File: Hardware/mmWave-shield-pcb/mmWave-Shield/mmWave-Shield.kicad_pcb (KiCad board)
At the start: 4 copper layers, 21 x 15 mm, 42 parts, among them J3 DF40HC_3.0_-40DS-0.4V_51, J4 DF40HC_3.0_-50DS-0.4V_51, U1 TPS22916CYFPR, U2 TPS22916CYFPR, X1 KC2016K80.0000C1GE00

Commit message: Cleaning up a bit
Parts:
- moved TP4 1.10 mm to (138.6, 105.2)
- moved TP5 1.10 mm to (139.7, 105.2)
- renumbered TP1 to DIV
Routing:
- net /sensor/sw_in_1v8: track 10.2 -> 11.4 mm
- net VD2: track 10.8 -> 11.8 mm
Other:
- board text added: "1V8"
- board text added: "3V3"

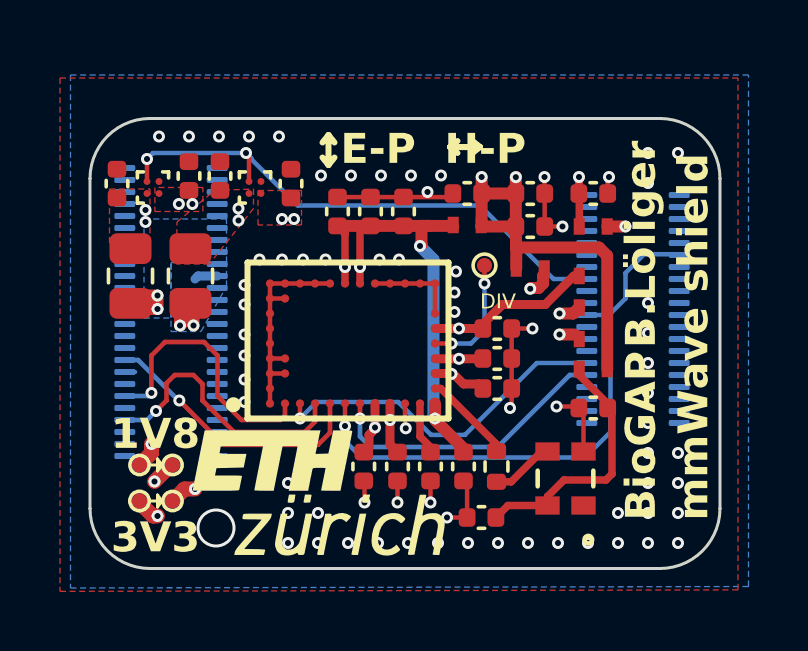
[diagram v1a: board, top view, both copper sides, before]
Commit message: Removed cap and rerouted some power lines
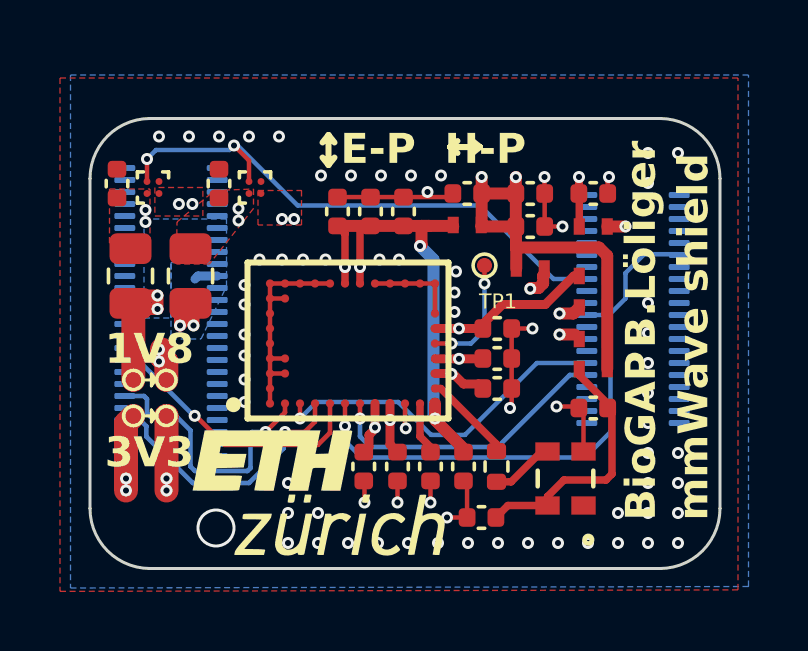
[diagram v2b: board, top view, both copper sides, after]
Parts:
- removed C17, C19: 47uF, Capacitor_SMD:C_0402_1005Metric
- C18, C20: value 1uF -> 4.7uF
- moved TP2 2.84 mm to (138.3, 103.6)
- moved TP3 2.84 mm to (139.4, 103.6)
- moved TP4 2.84 mm to (138.3, 102.4)
- moved TP5 2.84 mm to (139.4, 102.4)
- moved C20 0.26 mm to (141.2, 95.8)
- renumbered DIV to TP1
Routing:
- net /sensor/sw_in_1v8: track 11.4 -> 6.64 mm, vias 3 -> 4
- net 1V8_Connector: track 8.95 -> 4.84 mm, vias 3 -> 2
- net /sensor/sw_in_3v3: track 11.0 -> 12.9 mm, vias 3 -> 4
- net VD2: track 11.8 -> 12.8 mm, vias 3 -> 4
- net nRF_P0.07/AMUX: track 18.2 -> 18.8 mm

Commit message: added 3d models for new components
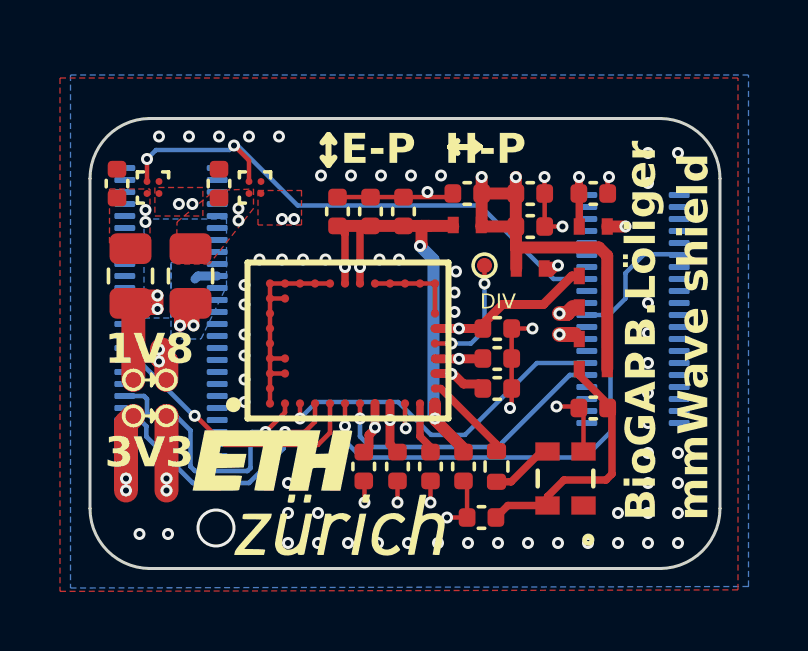
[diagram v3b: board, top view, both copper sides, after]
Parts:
- renumbered TP1 to DIV
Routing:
- net VDD_PLL: track 5.99 -> 7.13 mm
- net GND: vias 69 -> 71
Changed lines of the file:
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@@
 		)
 		(embedded_fonts no)
+		(model "${KIPRJMOD}/extra components/TPS22916CYFPR/TPS22916CYFPR.step"
+			(offset
+				(xyz 0 0 -0.2)
+			)
+			(scale
+				(xyz 1 1 1)
+			)
+			(rotate
+				(xyz -90 -0 -0)
+			)
+		)
 	)
 	(footprint "MMZ1005S121CT000:IND_1005_TDK-L"
@@
 		(descr "SMD pad as test Point, diameter 1.0mm")
 		(tags "test point SMD pad")
-		(property "Reference" "TP1"
+		(property "Reference" "DIV"
 			(at 0.45 1.2 0)
 			(layer "F.SilkS")
@@
 		)
 		(embedded_fonts no)
+		(model "${KIPRJMOD}/extra components/TPS22916CYFPR/TPS22916CYFPR.step"
+			(offset
+				(xyz 0 0 -0.2)
+			)
+			(scale
+				(xyz 1 1 1)
+			)
+			(rotate
+				(xyz -90 -0 -0)
+			)
+		)
 	)
 	(footprint "Resistor_SMD:R_0805_2012Metric"
@@
 		)
 		(embedded_fonts no)
+		(model "${KIPRJMOD}/extra components/KC2016K80_0000C1GE00/KC2016K_KYO.step"
+			(offset
+				(xyz 0 0 0)
+			)
+			(scale
+				(xyz 1 1 1)
+			)
+			(rotate
+				(xyz 0 0 0)
+			)
+		)
 	)
 	(footprint "Capacitor_SMD:C_0402_1005Metric"
@@
 	)
 	(via
+		(at 139.5 107.5)
+		(size 0.4)
+		(drill 0.2)
+		(layers "F.Cu" "B.Cu")
+		(free yes)
+		(net 2)
+	)
+	(via
 		(at 155.5 107.8)
 		(size 0.4)
@@
 	)
 	(via
+		(at 138.55 107.5)
+		(size 0.4)
+		(drill 0.2)
+		(layers "F.Cu" "B.Cu")
+		(free yes)
+		(net 2)
+	)
+	(via
 		(at 143.5 106.8)
 		(size 0.4)
@@
 	)
 	(segment
-		(start 153.2088 98.9)
-		(end 153.025 98.9)
+		(start 152.0125 99.85)
+		(end 150.65 99.85)
 		(width 0.3)
 		(layer "F.Cu")
@@
 	)
 	(segment
-		(start 150.65 99.85)
-		(end 149.995 100.505)
+		(start 149.2 100.65)
+		(end 149.995 100.65)
 		(width 0.3)
 		(layer "F.Cu")
@@
 	)
 	(segment
-		(start 149.2 100.65)
-		(end 149.995 100.65)
+		(start 152.9625 98.9)
+		(end 152.0125 99.85)
 		(width 0.3)
 		(layer "F.Cu")
@@
 	)
 	(segment
-		(start 152.075 99.85)
-		(end 150.65 99.85)
-		(width 0.3)
+		(start 149.995 100.505)
+		(end 149.995 100.55)
+		(width 0.25)
 		(layer "F.Cu")
 		(net 3)
 	)
 	(segment
-		(start 149.995 100.505)
-		(end 149.995 100.55)
-		(width 0.25)
+		(start 153.2088 98.9)
+		(end 152.9625 98.9)
+		(width 0.3)
 		(layer "F.Cu")
 		(net 3)
 	)
 	(segment
-		(start 153.025 98.9)
-		(end 152.075 99.85)
+		(start 150.65 99.85)
+		(end 149.995 100.505)
 		(width 0.3)
 		(layer "F.Cu")
@@
 	)
 	(segment
-		(start 152.0412 98.8588)
-		(end 152.0412 98.65)
-		(width 0.25)
+		(start 149.984322 101.660678)
+		(end 149.995 101.65)
+		(width 0.15)
 		(layer "F.Cu")
 		(net 5)
 	)
 	(segment
-		(start 151.6 99.3)
-		(end 151.85 99.3)
-		(width 0.4)
+		(start 152.500521 98.549479)
+		(end 152.250521 98.549479)
+		(width 0.25)
 		(layer "F.Cu")
 		(net 5)
 	)
 	(segment
-		(start 151.575 99.325)
-		(end 151.6 99.3)
-		(width 0.4)
+		(start 152.25 98.8)
+		(end 152.1 98.65)
+		(width 0.25)
 		(layer "F.Cu")
 		(net 5)
 	)
 	(segment
-		(start 149.984322 101.660678)
-		(end 149.995 101.65)
-		(width 0.15)
+		(start 152.1 98.65)
+		(end 152.0412 98.65)
+		(width 0.25)
 		(layer "F.Cu")
 		(net 5)
@@
 	)
 	(segment
-		(start 152.0052 99.1448)
-		(end 152.0052 98.8948)
-		(width 0.4)
-		(layer "F.Cu")
-		(net 5)
-	)
-	(segment
-		(start 151.85 99.3)
-		(end 152.0052 99.1448)
-		(width 0.4)
-		(layer "F.Cu")
-		(net 5)
-	)
-	(segment
-		(start 152.0052 98.8948)
-		(end 152.0412 98.8588)
-		(width 0.4)
+		(start 152.500521 98.549479)
+		(end 152.25 98.8)
+		(width 0.25)
 		(layer "F.Cu")
 		(net 5)
@@
 	)
 	(via
-		(at 151.575 99.325)
+		(at 152.500521 98.549479)
 		(size 0.4)
 		(drill 0.2)
@@
 	)
 	(segment
-		(start 151.575 99.325)
-		(end 151.55 99.35)
+		(start 152.500521 98.549479)
+		(end 152.350521 98.549479)
 		(width 0.25)
 		(layer "In2.Cu")
@@
 	)
 	(segment
-		(start 151.55 99.35)
-		(end 151.5 99.35)
-		(width 0.25)
+		(start 152.400521 98.549479)
+		(end 152.500521 98.549479)
+		(width 0.5)
 		(layer "In2.Cu")
 		(net 5)
 	)
 	(segment
-		(start 151.15 99.75)
-		(end 151.575 99.325)
+		(start 151.150057 99.799943)
+		(end 152.400521 98.549479)
 		(width 0.5)
 		(layer "In2.Cu")
@@
 	)
 	(segment
-		(start 151.15 99.799943)
-		(end 149.285107 101.664836)
+		(start 149.285107 101.664836)
+		(end 151.15 99.799943)
 		(width 0.5)
 		(layer "In2.Cu")
@@
 	(segment
 		(start 151.15 99.799943)
-		(end 151.15 99.75)
+		(end 151.150057 99.799943)
 		(width 0.5)
 		(layer "In2.Cu")
@@
 	)
 	(segment
-		(start 153.0088 100.15)
-		(end 153.2088 99.95)
-		(width 0.4)
-		(layer "F.Cu")
-		(net 6)
-	)
-	(segment
 		(start 146.9 103.15)
 		(end 146.9 103.7)
@@
 	(segment
 		(start 152.55 100.15)
-		(end 153.0088 100.15)
-		(width 0.4)
+		(end 152.8 100.15)
+		(width 0.5)
+		(layer "F.Cu")
+		(net 6)
+	)
+	(segment
+		(start 152.8 100.15)
+		(end 153 99.95)
+		(width 0.5)
 		(layer "F.Cu")
 		(net 6)
@@
 	)
 	(segment
-		(start 144.799 103.651057)
-		(end 145.750057 102.7)
-		(width 0.5)
-		(layer "In2.Cu")
-		(net 6)
-	)
-	(segment
-		(start 152.7 100)
-		(end 152.75 100)
+		(start 153.8 103.8)
+		(end 151.85 105.75)
 		(width 0.5)
 		(layer "In2.Cu")
@@
 	)
 	(segment
-		(start 152.75 100)
-		(end 153.8 101.05)
+		(start 146.9 103.25)
+		(end 146.9 103.600057)
 		(width 0.5)
 		(layer "In2.Cu")
@@
 	)
 	(segment
-		(start 152.55 100.15)
-		(end 152.7 100)
+		(start 146.35 102.7)
+		(end 146.9 103.25)
 		(width 0.5)
 		(layer "In2.Cu")
@@
 	)
 	(segment
-		(start 145.750057 102.7)
-		(end 146.35 102.7)
+		(start 153.8 101.05)
+		(end 153.8 103.8)
 		(width 0.5)
 		(layer "In2.Cu")
@@
 	)
 	(segment
-		(start 146.35 102.7)
-		(end 146.9 103.25)
+		(start 145.750057 102.7)
+		(end 146.35 102.7)
 		(width 0.5)
 		(layer "In2.Cu")
@@
 	)
 	(segment
-		(start 153.8 101.05)
-		(end 153.8 103.8)
+		(start 152.55 100.15)
+		(end 152.9 100.15)
 		(width 0.5)
 		(layer "In2.Cu")
@@
 	)
 	(segment
-		(start 153.8 103.8)
-		(end 151.85 105.75)
+		(start 144.799 105.049)
+		(end 144.799 103.651057)
 		(width 0.5)
 		(layer "In2.Cu")
@@
 	)
 	(segment
-		(start 144.799 105.049)
-		(end 144.799 103.651057)
+		(start 144.799 103.651057)
+		(end 145.750057 102.7)
 		(width 0.5)
 		(layer "In2.Cu")
@@
 	)
 	(segment
-		(start 146.9 103.25)
-		(end 146.9 103.600057)
+		(start 145.5 105.75)
+		(end 144.799 105.049)
 		(width 0.5)
 		(layer "In2.Cu")
@@
 	)
 	(segment
-		(start 145.5 105.75)
-		(end 144.799 105.049)
+		(start 152.9 100.15)
+		(end 153.8 101.05)
 		(width 0.5)
 		(layer "In2.Cu")
@@
 		(start 152.55 100.85)
 		(end 153.0588 100.85)
-		(width 0.4)
+		(width 0.5)
 		(layer "F.Cu")
 		(net 7)

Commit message: Final Touches and genertated fabrication files
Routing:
- net VDD_A: track 21.3 -> 14.5 mm
- net GAP_GPIO46: track 19.0 -> 23.2 mm
- net nRF_P1.11_GAP_GPIO63: track 9.80 -> 13.1 mm
- net nRF_P0.12_GAP_GPIO64: track 11.7 -> 14.9 mm
- net VDD_RF: track 17.1 -> 19.8 mm, vias 4 -> 2
- net VDD_LF: track 13.3 -> 11.2 mm
- net GND: track 28.2 -> 26.2 mm
- net VDD_D: track 10.6 -> 12.1 mm
- net VDD_PLL: track 7.13 -> 7.92 mm
- net VDD_VCO: vias 1 -> 0
